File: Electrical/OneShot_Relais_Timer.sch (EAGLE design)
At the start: 15 parts, among them IC2 ATTINY204SOIC14, K1 RE030012, T1 BC847, X1 MKDSN1,5/3-5,08

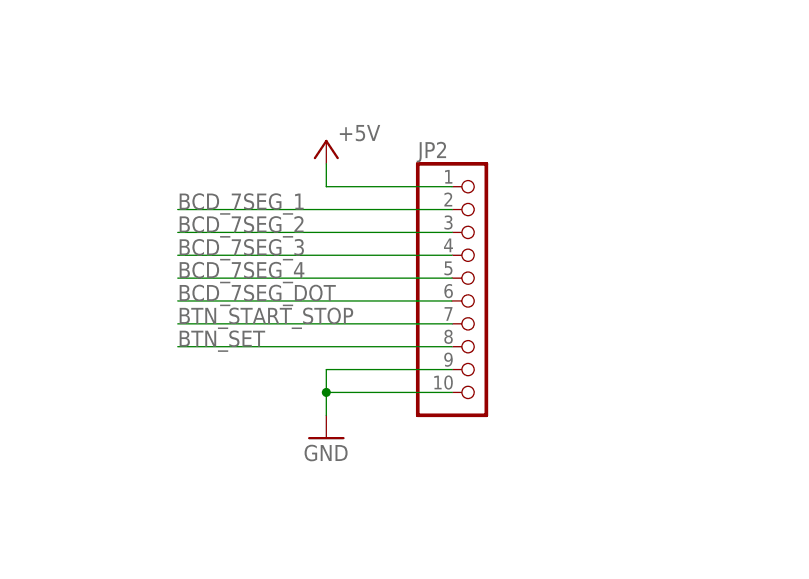
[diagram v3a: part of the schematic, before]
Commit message: Added mounting holes to PCB, moved relay, small adaptions to UI PCB
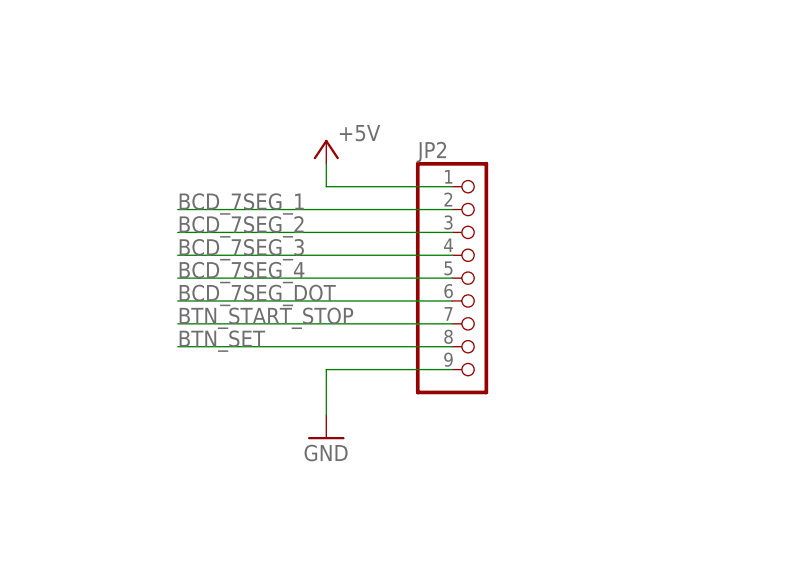
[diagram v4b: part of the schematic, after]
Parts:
- JP2: device pinhead:PINHD-1X10 -> pinhead:PINHD-1X9
- LED1: device OwnDevices:LEDCHIP-LED0603 -> led:LED5MM
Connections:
- net GND: no longer JP2.10
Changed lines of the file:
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@@
 <setting verticaltext="up"/>
 </settings>
-<grid distance="50" unitdist="mil" unit="mil" style="lines" multiple="1" display="no" altdistance="0.01" altunitdist="inch" altunit="inch"/>
+<grid distance="0.1" unitdist="inch" unit="inch" style="lines" multiple="1" display="no" altdistance="0.01" altunitdist="inch" altunit="inch"/>
 <layers>
 <layer number="1" name="Top" color="4" fill="1" visible="no" active="no"/>
@@
 <part name="R1" library="OwnDevices" library_urn="urn:adsk.eagle:library:19498084" deviceset="R-EU_" device="R0805" package3d_urn="urn:adsk.eagle:package:23553/2" value="10k"/>
 <part name="R2" library="OwnDevices" library_urn="urn:adsk.eagle:library:19498084" deviceset="R-EU_" device="R0805" package3d_urn="urn:adsk.eagle:package:23553/2" value="680"/>
-<part name="LED1" library="OwnDevices" library_urn="urn:adsk.eagle:library:19498084" deviceset="LED" device="CHIP-LED0603" package3d_urn="urn:adsk.eagle:package:15819/3"/>
+<part name="LED1" library="led" library_urn="urn:adsk.eagle:library:259" deviceset="LED" device="5MM" package3d_urn="urn:adsk.eagle:package:15799/2"/>
 <part name="T1" library="transistor" library_urn="urn:adsk.eagle:library:402" deviceset="BC847" device="" package3d_urn="urn:adsk.eagle:package:28738/2"/>
 <part name="D1" library="diode" library_urn="urn:adsk.eagle:library:210" deviceset="DIODE-" device="SOD80C" package3d_urn="urn:adsk.eagle:package:43405/2"/>
@@
 <part name="DA2" library="regulators-linear" deviceset="78L05" device="SOT223"/>
 <part name="TR1" library="OwnDevices" library_urn="urn:adsk.eagle:library:19498084" deviceset="EI30-12.5" device="" package3d_urn="urn:adsk.eagle:package:37656560/4"/>
-<part name="JP2" library="pinhead" library_urn="urn:adsk.eagle:library:325" deviceset="PINHD-1X10" device="" package3d_urn="urn:adsk.eagle:package:22406/2"/>
+<part name="JP2" library="pinhead" library_urn="urn:adsk.eagle:library:325" deviceset="PINHD-1X9" device="" package3d_urn="urn:adsk.eagle:package:22483/2"/>
 <part name="P+8" library="supply1" library_urn="urn:adsk.eagle:library:371" deviceset="+5V" device=""/>
 <part name="GND12" library="supply1" library_urn="urn:adsk.eagle:library:371" deviceset="GND" device=""/>
@@
 <wire x1="220.98" y1="76.2" x2="207.01" y2="76.2" width="0.1524" layer="91"/>
 <pinref part="GND12" gate="1" pin="GND"/>
-<wire x1="207.01" y1="76.2" x2="207.01" y2="73.66" width="0.1524" layer="91"/>
-<pinref part="JP2" gate="A" pin="10"/>
-<wire x1="207.01" y1="73.66" x2="207.01" y2="71.12" width="0.1524" layer="91"/>
-<wire x1="220.98" y1="73.66" x2="207.01" y2="73.66" width="0.1524" layer="91"/>
-<junction x="207.01" y="73.66"/>
-</segment>
-</net>
+<wire x1="207.01" y1="76.2" x2="207.01" y2="71.12" width="0.1524" layer="91"/>
+</segment>
+</net>

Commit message: Added 3D model for C1 on PCB, improved routing of PCB
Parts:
- C1: device rc-master-smd:CP_SV-G -> OwnDevices:CP_
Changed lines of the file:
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@@
 <part name="GND7" library="supply1" library_urn="urn:adsk.eagle:library:371" deviceset="GND" device=""/>
 <part name="GND8" library="supply1" library_urn="urn:adsk.eagle:library:371" deviceset="GND" device=""/>
-<part name="C1" library="rc-master-smd" deviceset="CP_" device="SV-G" value="1000u"/>
+<part name="C1" library="OwnDevices" library_urn="urn:adsk.eagle:library:19498084" deviceset="CP_" device="" package3d_urn="urn:adsk.eagle:package:37698300/2" value="1000u"/>
 <part name="GND9" library="supply1" library_urn="urn:adsk.eagle:library:371" deviceset="GND" device=""/>
 <part name="B1" library="rectifier" library_urn="urn:adsk.eagle:library:336" deviceset="DB?*G" device="S10" package3d_urn="urn:adsk.eagle:package:23898/1" technology="4"/>

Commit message: Small adaptions to PCBs, schematics, and mechanical components
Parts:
- R1: value 10k -> 1k
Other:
- note added: "Connector to UI PCB"
- note added: "HW_v1"
- note added: "Mains Relay"
- note added: "Microcontroller"
- note added: "Power Supply"
- moved on the sheet: B1, C1, D1, DA1, DA2, IC2, JP1, JP2, K1, LED1, R1, R2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
